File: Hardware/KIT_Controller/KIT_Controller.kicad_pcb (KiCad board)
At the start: 2 copper layers, 1 part, among them U1 LCD

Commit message: Satisfy constraints
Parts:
- added C1: 4.7uf, Capacitor_SMD:C_0805_2012Metric, F.Cu at (143.0, 83.0)
- added JP1: SolderJumper_2_Open, Jumper:SolderJumper-2_P1.3mm_Open_TrianglePad1.0x1.5mm, F.Cu at (149.3, 99.0)
- U1: value LCD -> Nokia_5110_LCD
- moved U1 2.89 mm to (146.0, 87.7)
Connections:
- U1 pad 2: unconnected-(U1-Pad2) -> Net-(C1-Pad1)
- U1 pad 3: unconnected-(U1-Pad3) -> GND
- U1 pad 4: unconnected-(U1-Pad4) -> Net-(JP1-Pad1)
- U1 pad 9: unconnected-(U1-Pad9) -> +3.3V

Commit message: fixup! Satisfy constraints
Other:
- board outline added: 72 x 72 mm
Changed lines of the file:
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@@
     )
   )
+  (gr_circle (center 145 107) (end 145 71) (layer "Edge.Cuts") (width 0.1) (fill none))
 )

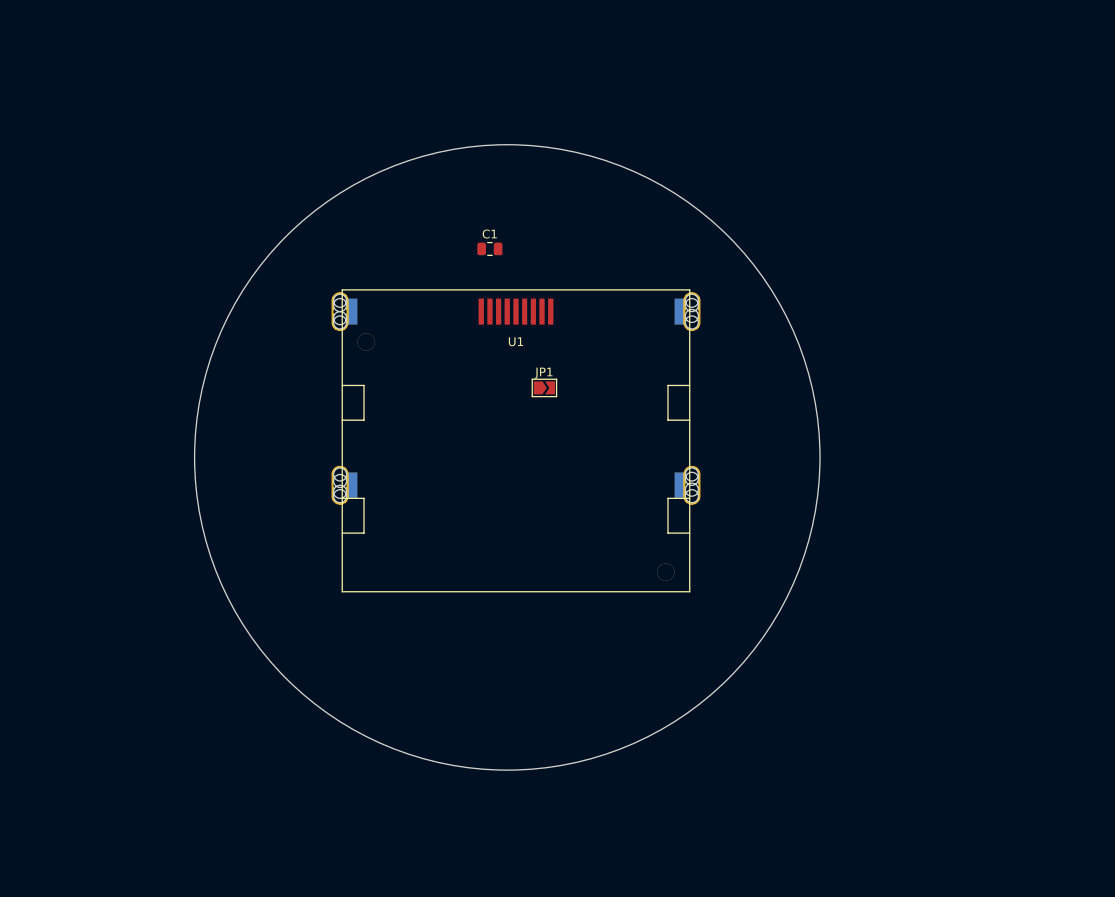
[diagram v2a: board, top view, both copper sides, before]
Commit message: Cleanup external libs and add extra bits to brd
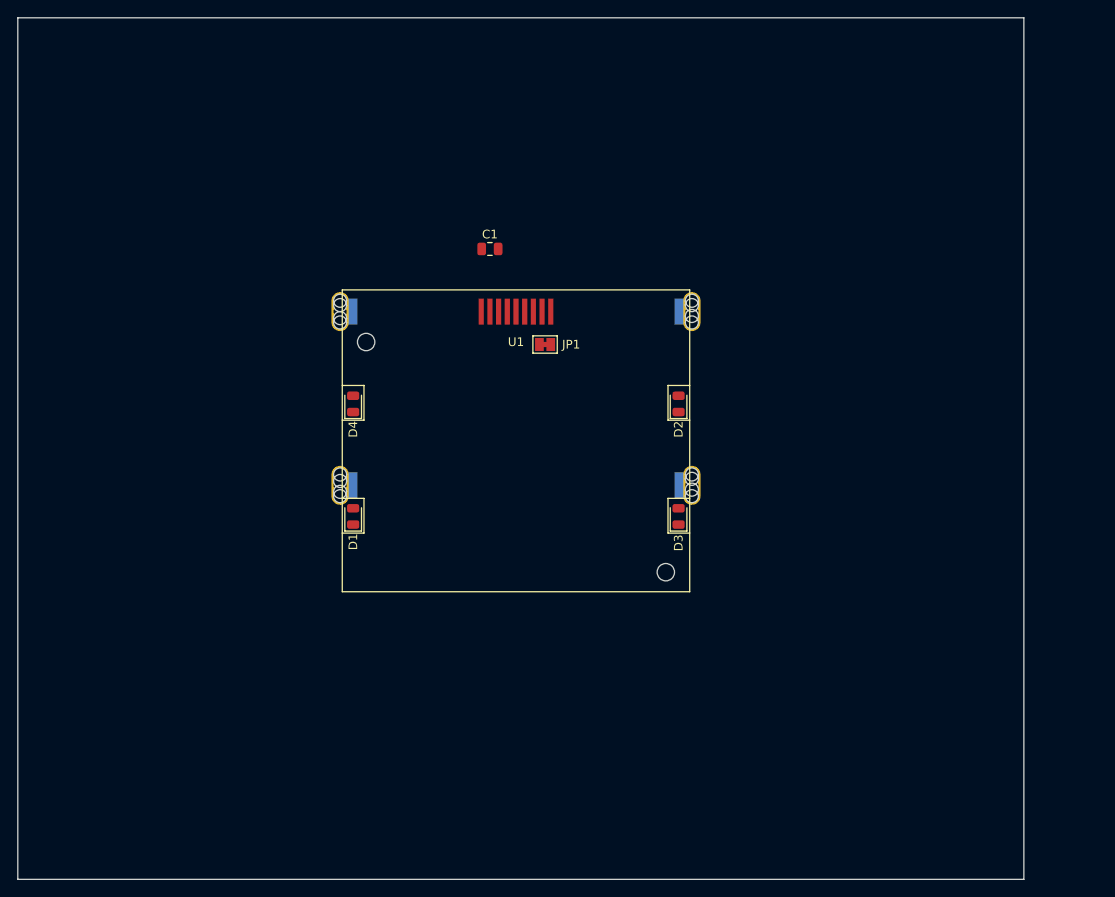
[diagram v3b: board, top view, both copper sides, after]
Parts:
- added D1: BL1, LED_SMD:LED_0805_2012Metric, F.Cu at (127.3, 113.8)
- added D2: BL2, LED_SMD:LED_0805_2012Metric, F.Cu at (164.7, 100.8)
- added D3: BL3, LED_SMD:LED_0805_2012Metric, F.Cu at (164.7, 113.8)
- added D4: BL4, LED_SMD:LED_0805_2012Metric, F.Cu at (127.3, 100.8)
- JP1: value SolderJumper_2_Open -> SolderJumper_2_Bridged; footprint Jumper:SolderJumper-2_P1.3mm_Open_TrianglePad1.0x1.5mm -> Jumper:SolderJumper-2_P1.3mm_Bridged_Pad1.0x1.5mm
- moved JP1 5.00 mm to (149.3, 94.0)
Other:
- board size 72 x 72 mm -> 115.8 x 99.2 mm

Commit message: Pad more components
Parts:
- added C101: 27p, Capacitor_SMD:C_0805_2012Metric, F.Cu at (106.2, 94.6)
- added C102: 27p, Capacitor_SMD:C_0805_2012Metric, F.Cu at (110.6, 94.6)
- added C103: 1u, Capacitor_SMD:C_0805_2012Metric, F.Cu at (110.2, 65.0)
- added C104: 100n, Capacitor_SMD:C_0805_2012Metric, F.Cu at (114.7, 71.0)
- added C105: 100n, Capacitor_SMD:C_0805_2012Metric, F.Cu at (105.8, 68.0)
- added C106: 100n, Capacitor_SMD:C_0805_2012Metric, F.Cu at (110.2, 71.0)
- added C107: 100n, Capacitor_SMD:C_0805_2012Metric, F.Cu at (119.1, 65.0)
- added C108: 100n, Capacitor_SMD:C_0805_2012Metric, F.Cu at (119.1, 68.0)
- added C109: 100n, Capacitor_SMD:C_0805_2012Metric, F.Cu at (105.8, 71.0)
- added C110: 100n, Capacitor_SMD:C_0805_2012Metric, F.Cu at (114.7, 65.0)
- added C111: 100n, Capacitor_SMD:C_0805_2012Metric, F.Cu at (114.7, 68.0)
- added C112: 100n, Capacitor_SMD:C_0805_2012Metric, F.Cu at (105.8, 65.0)
- added C113: 1u, Capacitor_SMD:C_0805_2012Metric, F.Cu at (110.2, 68.0)
- added R101: 1k, Resistor_SMD:R_0805_2012Metric, F.Cu at (119.1, 71.0)
- added R102: 27, Resistor_SMD:R_0805_2012Metric, F.Cu at (127.9, 75.8)
- added R103: 27, Resistor_SMD:R_0805_2012Metric, F.Cu at (123.5, 75.8)
- added U101: RP2040, Package_DFN_QFN:QFN-56-1EP_7x7mm_P0.4mm_EP3.2x3.2mm_ThermalVias, F.Cu at (112.1, 79.8)
- added Y101: Crystal, Crystal:Crystal_SMD_HC49-SD, F.Cu at (111.3, 90.0)
- renumbered C1 to C114, D1 to D101, D2 to D102, D3 to D103, D4 to D104, JP1 to JP101, U1 to U102
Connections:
- net +3.3V renamed +3V3

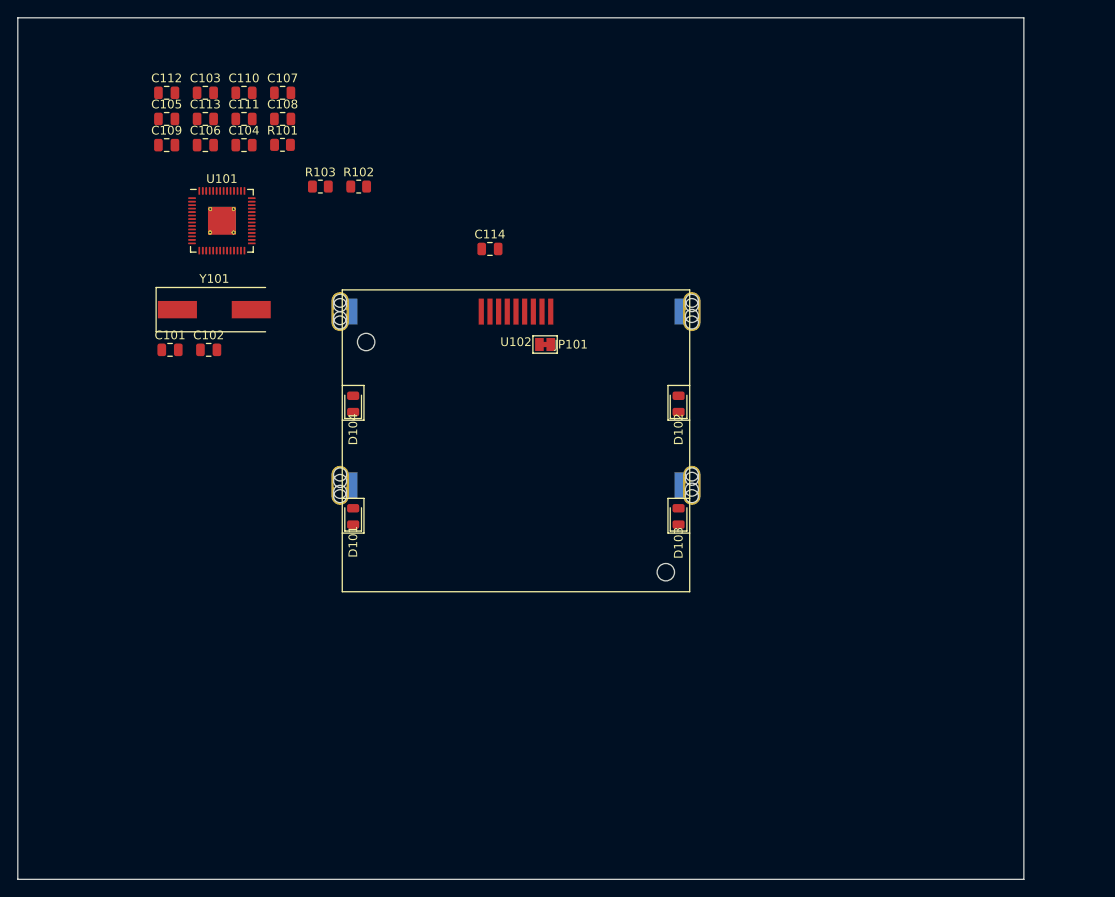
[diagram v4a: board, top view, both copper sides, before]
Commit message: Move MCU to its own schem
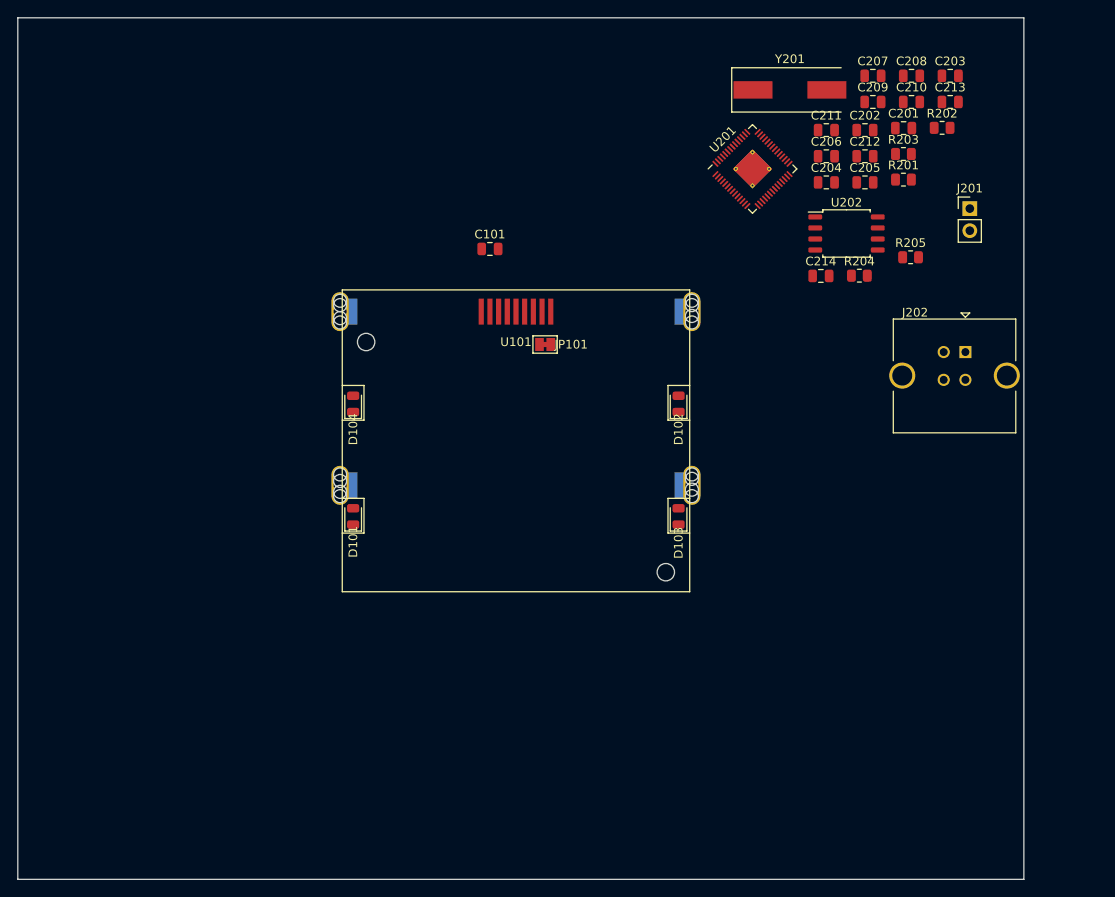
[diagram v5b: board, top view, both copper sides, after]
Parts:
- removed the C101 at (106.2, 94.6)
- removed C102: 27p, Capacitor_SMD:C_0805_2012Metric
- removed C103, C113: 1u, Capacitor_SMD:C_0805_2012Metric
- removed C104, C105, C106, C107, C108, C109, C110, C111, C112: 100n, Capacitor_SMD:C_0805_2012Metric
- removed R101: 1k, Resistor_SMD:R_0805_2012Metric
- removed R102, R103: 27, Resistor_SMD:R_0805_2012Metric
- removed the U101 at (112.1, 79.8)
- removed Y101: Crystal, Crystal:Crystal_SMD_HC49-SD
- added C201: 27p, Capacitor_SMD:C_0805_2012Metric, F.Cu at (190.6, 69.1)
- added C202: 27p, Capacitor_SMD:C_0805_2012Metric, F.Cu at (186.2, 69.3)
- added C203: 1u, Capacitor_SMD:C_0805_2012Metric, F.Cu at (196.0, 63.1)
- added C204: 100n, Capacitor_SMD:C_0805_2012Metric, F.Cu at (181.7, 75.3)
- added C205: 100n, Capacitor_SMD:C_0805_2012Metric, F.Cu at (186.2, 75.3)
- added C206: 100n, Capacitor_SMD:C_0805_2012Metric, F.Cu at (181.7, 72.3)
- added C207: 100n, Capacitor_SMD:C_0805_2012Metric, F.Cu at (187.1, 63.1)
- added C208: 100n, Capacitor_SMD:C_0805_2012Metric, F.Cu at (191.5, 63.1)
- added C209: 100n, Capacitor_SMD:C_0805_2012Metric, F.Cu at (187.1, 66.1)
- added C210: 100n, Capacitor_SMD:C_0805_2012Metric, F.Cu at (191.5, 66.1)
- added C211: 100n, Capacitor_SMD:C_0805_2012Metric, F.Cu at (181.7, 69.3)
- added C212: 100n, Capacitor_SMD:C_0805_2012Metric, F.Cu at (186.2, 72.3)
- added C213: 1u, Capacitor_SMD:C_0805_2012Metric, F.Cu at (196.0, 66.1)
- added C214: 100n, Capacitor_SMD:C_0805_2012Metric, F.Cu at (181.1, 86.1)
- added J201: USB_BOOT, Connector_PinHeader_2.54mm:PinHeader_1x02_P2.54mm_Vertical, F.Cu at (198.2, 78.4)
- added J202: USB_B, Connector_USB:USB_B_TE_5787834_Vertical, F.Cu at (197.7, 94.9)
- added R201: 1k, Resistor_SMD:R_0805_2012Metric, F.Cu at (190.6, 75.0)
- added R202: 27, Resistor_SMD:R_0805_2012Metric, F.Cu at (195.1, 69.1)
- added R203: 27, Resistor_SMD:R_0805_2012Metric, F.Cu at (190.6, 72.1)
- added R204: 1k, Resistor_SMD:R_0805_2012Metric, F.Cu at (185.5, 86.1)
- added R205: DNP, Resistor_SMD:R_0805_2012Metric, F.Cu at (191.4, 84.0)
- added U201: RP2040, Package_DFN_QFN:QFN-56-1EP_7x7mm_P0.4mm_EP3.2x3.2mm_ThermalVias, F.Cu at (173.2, 73.8)
- added U202: W25Q128JVS, Package_SO:SOIC-8_5.23x5.23mm_P1.27mm, F.Cu at (184.1, 81.2)
- added Y201: Crystal, Crystal:Crystal_SMD_HC49-SD, F.Cu at (177.5, 64.7)
- renumbered C114 to C101, U102 to U101

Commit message: add other junk idk
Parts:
- added C203: 10u, Capacitor_SMD:C_0805_2012Metric, F.Cu at (190.6, 121.0)
- added C205: 10u, Capacitor_SMD:C_0805_2012Metric, F.Cu at (195.1, 121.0)
- added R101: 450, Resistor_SMD:R_0805_2012Metric, F.Cu at (175.6, 143.1)
- added R102: 450, Resistor_SMD:R_0805_2012Metric, F.Cu at (171.1, 143.1)
- added R103: 450, Resistor_SMD:R_0805_2012Metric, F.Cu at (171.1, 140.1)
- added R104: 450, Resistor_SMD:R_0805_2012Metric, F.Cu at (175.6, 140.1)
- added U201: TCA9554DB, Package_SO:SSOP-16_5.3x6.2mm_P0.65mm, F.Cu at (183.3, 123.4)
- added U203: NCP1117-3.3_SOT223, Package_TO_SOT_SMD:SOT-223-3_TabPin2, F.Cu at (183.2, 131.4)
- added U204: HDSP-7401, Display_7Segment:HDSP-7401, F.Cu at (171.1, 121.7)
- J201: renamed from J202; footprint Connector_USB:USB_B_TE_5787834_Vertical -> Connector_USB:USB_B_OST_USB-B1HSxx_Horizontal
- renumbered C214 to C204, C203 to C206, C204 to C207, C205 to C208, C206 to C209, C207 to C210, C208 to C211, C209 to C212, C210 to C213, C211 to C214, C212 to C215, C213 to C216, J201 to J202, R204 to R201, R205 to R202, R201 to R203, R202 to R204, R203 to R205, U201 to U205
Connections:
- D101 pad 1: unconnected-(D101-Pad1) -> +3V3
- D101 pad 2: unconnected-(D101-Pad2) -> Net-(D101-Pad2)
- D102 pad 1: unconnected-(D102-Pad1) -> +3V3
- D102 pad 2: unconnected-(D102-Pad2) -> Net-(D102-Pad2)
- D103 pad 1: unconnected-(D103-Pad1) -> +3V3
- D103 pad 2: unconnected-(D103-Pad2) -> Net-(D103-Pad2)
- D104 pad 1: unconnected-(D104-Pad1) -> +3V3
- D104 pad 2: unconnected-(D104-Pad2) -> Net-(D104-Pad2)
- J201 pad 1: unconnected-(J202-Pad1) -> VBUS
- J201 pad 2: unconnected-(J202-Pad2) -> /MCU/USB_D-
- J201 pad 3: unconnected-(J202-Pad3) -> /MCU/USB_D+
- J201 pad 4: unconnected-(J202-Pad4) -> GND
- J201 pad 5: unconnected-(J202-Pad5) -> GND

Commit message: Add more stuff
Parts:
- added R206: 10k, Resistor_SMD:R_0805_2012Metric, F.Cu at (106.9, 100.0)
- added R207: 240, Resistor_SMD:R_0805_2012Metric, F.Cu at (106.9, 97.0)
- added R208: 240, Resistor_SMD:R_0805_2012Metric, F.Cu at (111.3, 103.0)
- added R209: 240, Resistor_SMD:R_0805_2012Metric, F.Cu at (102.5, 97.0)
- added R210: 240, Resistor_SMD:R_0805_2012Metric, F.Cu at (111.3, 97.0)
- added R211: 240, Resistor_SMD:R_0805_2012Metric, F.Cu at (102.5, 103.0)
- added R212: 240, Resistor_SMD:R_0805_2012Metric, F.Cu at (106.9, 103.0)
- added R213: 240, Resistor_SMD:R_0805_2012Metric, F.Cu at (102.5, 100.0)
- added R214: 240, Resistor_SMD:R_0805_2012Metric, F.Cu at (111.3, 100.0)
- moved U201 81.0 mm to (109.5, 90.0)
- moved U204 64.2 mm to (116.5, 88.0)
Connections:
- U201 pad 1: unconnected-(U201-Pad1) -> GND
- U201 pad 10: unconnected-(U201-Pad10) -> Net-(U201-Pad10)
- U201 pad 11: unconnected-(U201-Pad11) -> Net-(U201-Pad11)
- U201 pad 12: unconnected-(U201-Pad12) -> Net-(U201-Pad12)
- U201 pad 14: unconnected-(U201-Pad14) -> /MCU/SCL
- U201 pad 15: unconnected-(U201-Pad15) -> /MCU/SDA
- U201 pad 16: unconnected-(U201-Pad16) -> +3V3
- U201 pad 2: unconnected-(U201-Pad2) -> GND
- U201 pad 3: unconnected-(U201-Pad3) -> GND
- U201 pad 4: unconnected-(U201-Pad4) -> Net-(U201-Pad4)
- U201 pad 5: unconnected-(U201-Pad5) -> Net-(U201-Pad5)
- U201 pad 6: unconnected-(U201-Pad6) -> Net-(U201-Pad6)
- U201 pad 7: unconnected-(U201-Pad7) -> Net-(U201-Pad7)
- U201 pad 8: unconnected-(U201-Pad8) -> GND
- U201 pad 9: unconnected-(U201-Pad9) -> Net-(U201-Pad9)
- U204 pad 1: unconnected-(U204-Pad1) -> GND
- U204 pad 10: unconnected-(U204-Pad10) -> Net-(U204-Pad10)
- U204 pad 2: unconnected-(U204-Pad2) -> Net-(U204-Pad2)
- U204 pad 3: unconnected-(U204-Pad3) -> Net-(U204-Pad3)
- U204 pad 4: unconnected-(U204-Pad4) -> Net-(U204-Pad4)
- U204 pad 5: unconnected-(U204-Pad5) -> Net-(U204-Pad5)
- U204 pad 6: unconnected-(U204-Pad6) -> GND
- U204 pad 7: unconnected-(U204-Pad7) -> Net-(U204-Pad7)
- U204 pad 8: unconnected-(U204-Pad8) -> Net-(U204-Pad8)
- U204 pad 9: unconnected-(U204-Pad9) -> Net-(U204-Pad9)
- U205 pad 6: unconnected-(U205-Pad6) -> /MCU/SDA
- U205 pad 7: unconnected-(U205-Pad7) -> /MCU/SCL
